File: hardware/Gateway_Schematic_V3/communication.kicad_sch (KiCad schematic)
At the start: 48 parts, among them J17 HR911105A, U9 W5500, Y2 25MHz

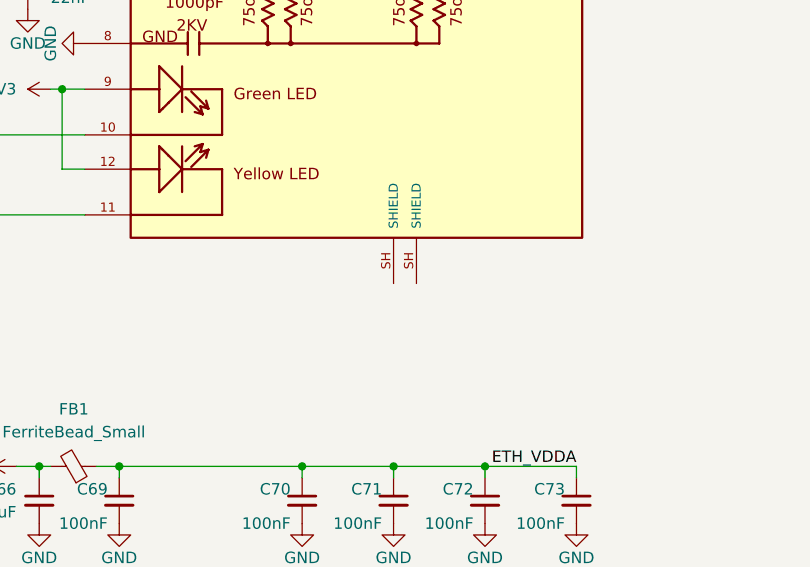
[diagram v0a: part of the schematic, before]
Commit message: Update PCB Layout for Gateway: change button, add gnd vias, fix silkscreen
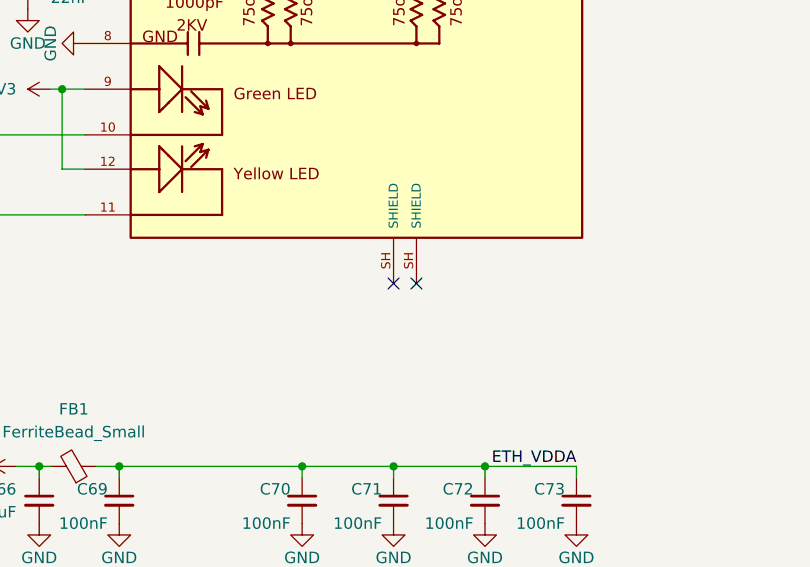
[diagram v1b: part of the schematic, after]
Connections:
- no-connect marks 3 -> 5
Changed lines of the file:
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@@
+	)
+	(no_connect
+		(at 228.6 139.7)
 	)
 	(no_connect
@@
 	)
 	(no_connect
+		(at 226.06 139.7)
+	)
+	(no_connect

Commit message: Update Capacital for Shield of Ethernet
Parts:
- added C74: 4.7nF, IVS_FOOTPRINTS:C_0603, symbol Device:C_Small
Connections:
- net GND: now also C74.2
- net at J17.SH (SHIELD): now also C74.1
- no-connect marks 5 -> 3
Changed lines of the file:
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@@
 	)
 	(junction
+		(at 227.33 140.97)
+		(diameter 0)
+		(color 0 0 0 0)
+	)
+	(junction
 		(at 87.63 142.24)
 		(diameter 0)
@@
 	)
 	(no_connect
-		(at 228.6 139.7)
-	)
-	(no_connect
 		(at 128.27 106.68)
 	)
@@
 	)
 	(no_connect
-		(at 226.06 139.7)
-	)
-	(no_connect
 		(at 128.27 111.76)
 	)
@@
 	(wire
 		(pts
+			(xy 226.06 140.97) (xy 227.33 140.97)
+		)
+		(stroke
+			(width 0)
+			(type default)
+		)
+	)
+	(wire
+		(pts
 			(xy 162.56 109.22) (xy 162.56 123.19)
 		)
@@
 	(wire
 		(pts
+			(xy 226.06 139.7) (xy 226.06 140.97)
+		)
+		(stroke
+			(width 0)
+			(type default)
+		)
+	)
+	(wire
+		(pts
 			(xy 92.71 134.62) (xy 92.71 135.89)
 		)
@@
 	(wire
 		(pts
+			(xy 228.6 139.7) (xy 228.6 140.97)
+		)
+		(stroke
+			(width 0)
+			(type default)
+		)
+	)
+	(wire
+		(pts
 			(xy 64.77 110.49) (xy 67.31 110.49)
 		)
@@
 	(wire
 		(pts
+			(xy 227.33 140.97) (xy 228.6 140.97)
+		)
+		(stroke
+			(width 0)
+			(type default)
+		)
+	)
+	(wire
+		(pts
 			(xy 152.4 86.36) (xy 152.4 88.9)
 		)
@@
 	(wire
 		(pts
+			(xy 227.33 140.97) (xy 227.33 142.24)
+		)
+		(stroke
+			(width 0)
+			(type default)
+		)
+	)
+	(wire
+		(pts
 			(xy 46.99 99.06) (xy 49.53 99.06)
 		)
@@
 	)
 	(symbol
+		(lib_id "power:GND")
+		(at 227.33 147.32 0)
+		(mirror y)
+		(unit 1)
+		(exclude_from_sim no)
+		(in_bom yes)
+		(on_board yes)
+		(dnp no)
+		(property "Reference" "#PWR0126"
+			(at 227.33 153.67 0)
+			(effects
+				(font
+					(size 1.27 1.27)
+				)
+				(hide yes)
+			)
+		)
+		(property "Value" "GND"
+			(at 227.33 151.13 0)
+			(effects
+				(font
+					(size 1.27 1.27)
+				)
+			)
+		)
+		(property "Footprint" ""
+			(at 227.33 147.32 0)
+			(effects
+				(font
+					(size 1.27 1.27)
+				)
+				(hide yes)
+			)
+		)
+		(property "Datasheet" ""
+			(at 227.33 147.32 0)
+			(effects
+				(font
+					(size 1.27 1.27)
+				)
+				(hide yes)
+			)
+		)
+		(property "Description" "Power symbol creates a global label with name \"GND\" , ground"
+			(at 227.33 147.32 0)
+			(effects
+				(font
+					(size 1.27 1.27)
+				)
+				(hide yes)
+			)
+		)
+		(pin "1"
+		)
+		(instances
+			(project "Gateway_Schematic_V3"
+				(path "/08b065f5-231d-43cb-bb9e-87dca43beac9/e826eac3-07a8-4403-aea2-c6706516015d"
+					(reference "#PWR0126")
+					(unit 1)
+				)
+			)
+		)
+	)
+	(symbol
 		(lib_id "Device:R_Small")
 		(at 142.24 78.74 90)
@@
 					(unit 1)
 				)
+			)
+		)
+	)
+	(symbol
+		(lib_id "Device:C_Small")
+		(at 227.33 144.78 0)
+		(mirror y)
+		(unit 1)
+		(exclude_from_sim no)
+		(in_bom yes)
+		(on_board yes)
+		(dnp no)
+		(property "Reference" "C74"
+			(at 226.06 143.51 0)
+			(effects
+				(font
+					(size 1.27 1.27)
+				)
+				(justify left)
+			)
+		)
+		(property "Value" "4.7nF"
+			(at 226.06 147.32 0)
+			(effects
+				(font
+					(size 1.27 1.27)
+				)
+				(justify left)
+			)
+		)
+		(property "Footprint" "IVS_FOOTPRINTS:C_0603"
+			(at 227.33 144.78 0)
+			(effects
+				(font
+					(size 1.27 1.27)
+				)
+				(hide yes)
+			)
+		)
+		(property "Datasheet" "~"
+			(at 227.33 144.78 0)
+			(effects
+				(font
+					(size 1.27 1.27)
+				)
+				(hide yes)
+			)
+		)
+		(property "Description" "Unpolarized capacitor, small symbol"
+			(at 227.33 144.78 0)
+			(effects
+				(font
+					(size 1.27 1.27)
+				)
+				(hide yes)
+			)
+		)
+		(pin "1"
+		)
+		(pin "2"
+		)
+		(instances
+			(project "Gateway_Schematic_V3"
+				(path "/08b065f5-231d-43cb-bb9e-87dca43beac9/e826eac3-07a8-4403-aea2-c6706516015d"
+					(reference "C74")
+					(unit 1)
+				)
